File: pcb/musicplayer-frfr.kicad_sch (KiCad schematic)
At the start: 22 parts, among them J1 Battery, J2 AudioPlug3, J3 Display, SW1 SW_Push, SW2 SW_Push, SW3 SW_Push, SW4 RotaryEncoder_Switch, U1 XIAO-RP2350-SMD, U2 TP4056-42-ESOP8, U3 DFPLAYER_MINI

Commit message: fix up pcb with cool new rounded corners and some layout changes. also added a power switch
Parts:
- added SW5: SW_SPDT, Button_Switch_THT:SW_Slide_SPDT_Straight_CK_OS102011MS2Q, symbol Switch:SW_SPDT
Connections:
- net VBAT: now also SW5.1 (A); no longer U1.29 (VBAT)
- new net XIAO_VBAT: SW5.2 (B), U1.29 (VBAT)
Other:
- moved on the sheet: C3, C4, J2, U1

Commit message: fix up pcb bcuz kicad didnt place the right parts. also added fabrication files
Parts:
- C1, C2, C3: LCSC PN (none) -> C88722
- C4: value 0.1u -> 100n; LCSC PN (none) -> C1711
- D1, D2: LCSC PN (none) -> C5353439
- J1: LCSC PN (none) -> C157932
- J2: LCSC PN (none) -> C4991872
- J3: LCSC PN (none) -> C7191451; MPN (none) -> 68604-804HLF
- R1: LCSC PN (none) -> C114521
- R2, R3, R4: LCSC PN (none) -> C844939
- R5, R6: LCSC PN (none) -> C844941
- SW1, SW2, SW3: LCSC PN (none) -> C557612; MPN (none) -> TS4550CJ
- SW4: LCSC PN (none) -> C202365; MPN (none) -> EC11E18244AU
- SW5: LCSC PN (none) -> C221829; MPN (none) -> OS102011MS2QN1
- U1: LCSC PN (none) -> C41882923; MPN (none) -> 102010550
- U2: LCSC PN (none) -> C16581; MPN (none) -> TP4056-42-ESOP8
- U3: LCSC PN (none) -> C5371690; MPN (none) -> DFR0299

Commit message: rework schemtaic to bet bigger badder and better
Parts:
- removed C1, C2, C3: 100u, Capacitor_THT:CP_Radial_D6.3mm_P2.50mm, symbol Device:C
- removed C4: 100n, Capacitor_SMD:C_0805_2012Metric, symbol Device:C
- removed D1, D2: LED, LED_SMD:LED_0805_2012Metric, symbol Device:LED
- removed J2: AudioPlug3, Connector_Audio:Jack_3.5mm_CUI_SJ-3523-SMT_Horizontal, symbol Connector_Audio:AudioPlug3
- removed R1: 2.4K, Resistor_SMD:R_0805_2012Metric, symbol Device:R
- removed R2: 1K, Resistor_SMD:R_0805_2012Metric, symbol Device:R
- removed SW4: RotaryEncoder_Switch, Rotary_Encoder:RotaryEncoder_Alps_EC11E-Switch_Vertical_H20mm, symbol Device:RotaryEncoder_Switch
- removed U2: TP4056-42-ESOP8, Package_SO:SOIC-8-1EP_3.9x4.9mm_P1.27mm_EP2.41x3.3mm_ThermalVias, symbol Battery_Management:TP4056-42-ESOP8
- removed U3: DFPLAYER_MINI, DFPlayer:DFPlayer_V2, symbol Arduino:DFPLAYER_MINI
- added D1, D2, D3, D4, D5, D6, D7, D8, D9: 1N4149, Diode_THT:D_DO-35_SOD27_P7.62mm_Horizontal, symbol Diode:1N4149
- added R7: 4.7k, symbol Device:R
- added SW10: Next, Button_Switch_THT:SW_PUSH_6mm, symbol Switch:SW_Push
- added SW4: Left, Button_Switch_THT:SW_PUSH_6mm, symbol Switch:SW_Push
- added SW6: Select, Button_Switch_THT:SW_PUSH_6mm, symbol Switch:SW_Push
- added SW7: Right, Button_Switch_THT:SW_PUSH_6mm, symbol Switch:SW_Push
- added SW8: Prev., Button_Switch_THT:SW_PUSH_6mm, symbol Switch:SW_Push
- added SW9: Down, Button_Switch_THT:SW_PUSH_6mm, symbol Switch:SW_Push
- added TP1: USB D-, symbol Connector:TestPoint
- added TP2: USB D+, symbol Connector:TestPoint
- added U4: ESP32-S3-WROOM-1, RF_Module:ESP32-S3-WROOM-1, symbol RF_Module:ESP32-S3-WROOM-1
- R3: value 1K -> 10k; footprint Resistor_SMD:R_0805_2012Metric -> (none); LCSC PN C844939 -> (none); MPN CRCW08051K00FKEA -> (none)
- R4: value 1K -> 4.7k; footprint Resistor_SMD:R_0805_2012Metric -> (none); LCSC PN C844939 -> (none); MPN CRCW08051K00FKEA -> (none)
- SW1: value SW_Push -> Vol Up
- SW2: value SW_Push -> Up
- SW3: value SW_Push -> Vol Down
- SW5: value SW_SPDT -> SW_BAT
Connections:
- net ENCODER_SWITCH is gone; now on net XIAO_RX: U1.15 (D11)
- net +3V3: now also J3.3 (VCC), R3.1, R4.1, R7.1, U4.2 (3V3)
- net BUSY: now also U1.1 (D0); no longer U1.16 (D12)
- net GND: now also U4.1 (GND), U4.40 (GND), U4.41 (GND); no longer R3.1, SW1.2, SW2.2, SW3.2
- net SCL: now also R7.2
- net SDA: now also R4.2
- net XIAO_RX: now also U4.37 (TXD0); no longer U1.7 (D6)
- net XIAO_TX: now also U1.16 (D12), U4.36 (RXD0); no longer R4.1, U1.8 (D7)
- net SPI_MISO: now reaches U1.10 (D9)
- net SPI_MISO: now also U4.21 (IO13)
- net SPI_MOSI: now reaches U1.11 (D10)
- net SPI_MOSI: now also U4.19 (IO11)
- net COL2: now reaches U1.19 (D15)
- net COL2: now also SW2.1, SW6.1, SW9.1
- net COL1: now reaches U1.20 (D16)
- net COL1: now also SW1.1, SW4.1, SW8.1
- net ROW3: now reaches U1.21 (D17)
- net ROW3: now also D7.1 (K), D8.1 (K), D9.1 (K)
- net ROW2: now reaches U1.22 (D18)
- net ROW2: now also D4.1 (K), D5.1 (K), D6.1 (K)
- net SPI_CS: now reaches U1.4 (D3)
- net SPI_CS: now also U4.18 (IO10)
- net SPI_SCK: now reaches U1.9 (D8)
- net SPI_SCK: now also U4.20 (IO12)
- net ESP_BOOT: now reaches R3.2
- net ESP_BOOT: now also U4.27 (IO0)
- net BACK: no longer names the net of U1.3 (D2)
- net BACK: no longer SW1.1
- net ENCODER_A: no longer names the net of U1.17 (D13)
- net ENCODER_B: no longer names the net of U1.18 (D14)
- net NEXT renamed COL3
- net COL3: now also SW10.1, SW7.1
- removed net PLAY: SW2.1, U1.1 (D0)
- net VBUS renamed +5V
- net +5V: no longer J3.3 (VCC)
- new net: D1.2 (A), SW1.2
- new net: D8.2 (A), SW9.2
- new net: D9.2 (A), SW10.2
- new net: D2.2 (A), SW2.2
- new net: TP1.1, U4.13 (USB_D-)
- new net: D5.2 (A), SW6.2
- new net: D4.2 (A), SW4.2
- new net: D6.2 (A), SW7.2
- new net: D7.2 (A), SW8.2
- new net: D3.2 (A), SW3.2
- new net: TP2.1, U4.14 (USB_D+)
- new net AMP_SDN: U4.39 (IO1)
- new net DAC_XSMT: U4.12 (IO8)
- new net ESP_ENABLE: U1.7 (D6), U4.3 (EN)
- new net I2S_BCK: U4.31 (IO38)
- new net I2S_DIN: U4.32 (IO39)
- new net I2S_LRCK: U4.33 (IO40)
- new net ROW1: D1.1 (K), D2.1 (K), D3.1 (K), U1.8 (D7)
- new net SD_CLK: U4.22 (IO14)
- new net SD_CMD: U4.8 (IO15)
- new net SD_D0: U4.38 (IO2)
- new net SD_D1: U4.4 (IO4)
- new net SD_D2: U4.5 (IO5)
- new net SD_D3: U4.6 (IO6)
- new net SD_DET: U4.7 (IO7)
- no-connect marks 19 -> 2
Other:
- added sheet Audio (audio.kicad_sch)
- added sheet SD Card (sd.kicad_sch)
- note added: "User Controls"
- moved on the sheet: J1, J3, R5, R6, SW1, SW2, SW3, SW5

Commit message: add RTC and stuff
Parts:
- added TP3, TP4, TP5, TP6: TestPoint, symbol Connector:TestPoint
- added U5: PCF8523T, Package_SO:SOIC-8_3.9x4.9mm_P1.27mm, symbol Timer_RTC:PCF8523T
- added Y1: 32.768 kHz, symbol Device:Crystal
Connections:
- net +3V3: now also TP6.1
- net +5V: now also TP4.1, U5.8 (VDD)
- net GND: now also TP3.1, U5.4 (VSS)
- net SCL: now also U5.6 (SCL)
- net SDA: now also U5.5 (SDA)
- net VBAT: now also TP5.1, U5.3 (VBAT)
- net INTA: now reaches U1.17 (D13)
- net INTA: now also U5.7 (~{INT1}/CLKOUT)
- net BUSY: no longer names the net of U1.1 (D0)
- new net: U5.1 (OSCI), Y1.1
- new net: U5.2 (OSCO), Y1.2
- no-connect marks 2 -> 22
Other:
- note added: "Audio"
- note added: "Battery stuff"
- note added: "Display"
- note added: "ESP32"
- note added: "RTC"
- note added: "SD Card"
- note added: "XIAO RP2350"
- moved on the sheet: D1, D2, D3, D4, D5, D6, D7, D8, D9, J1, J3, R3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

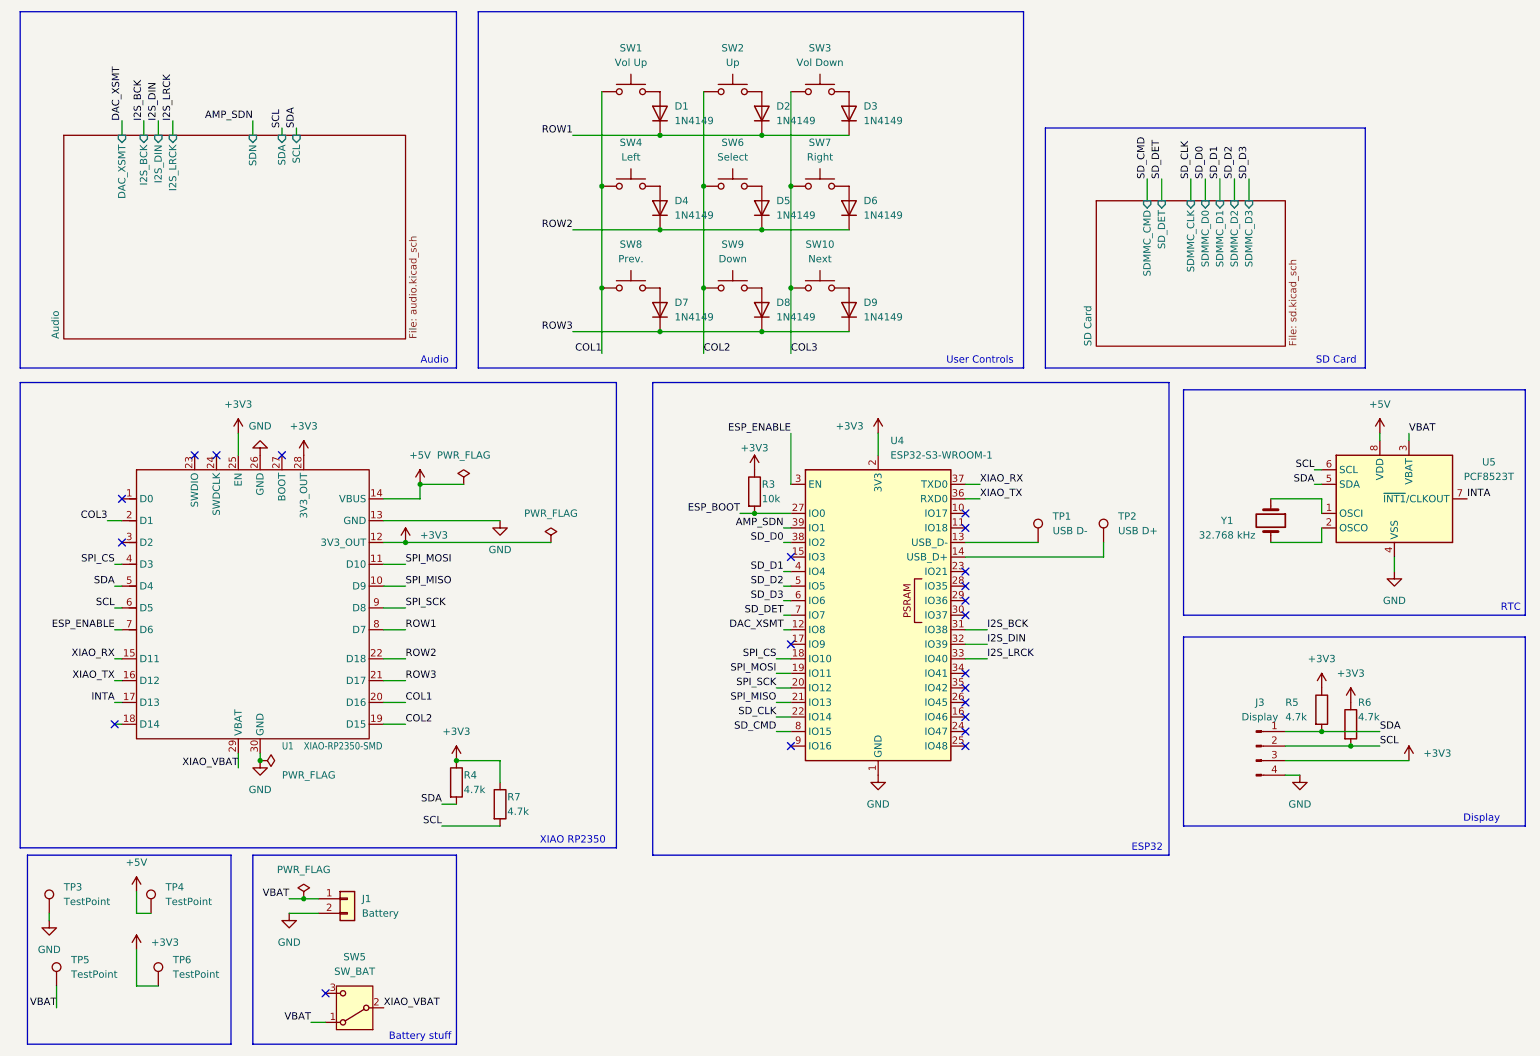
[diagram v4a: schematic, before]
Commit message: fix JOURNAL.md hour formatting
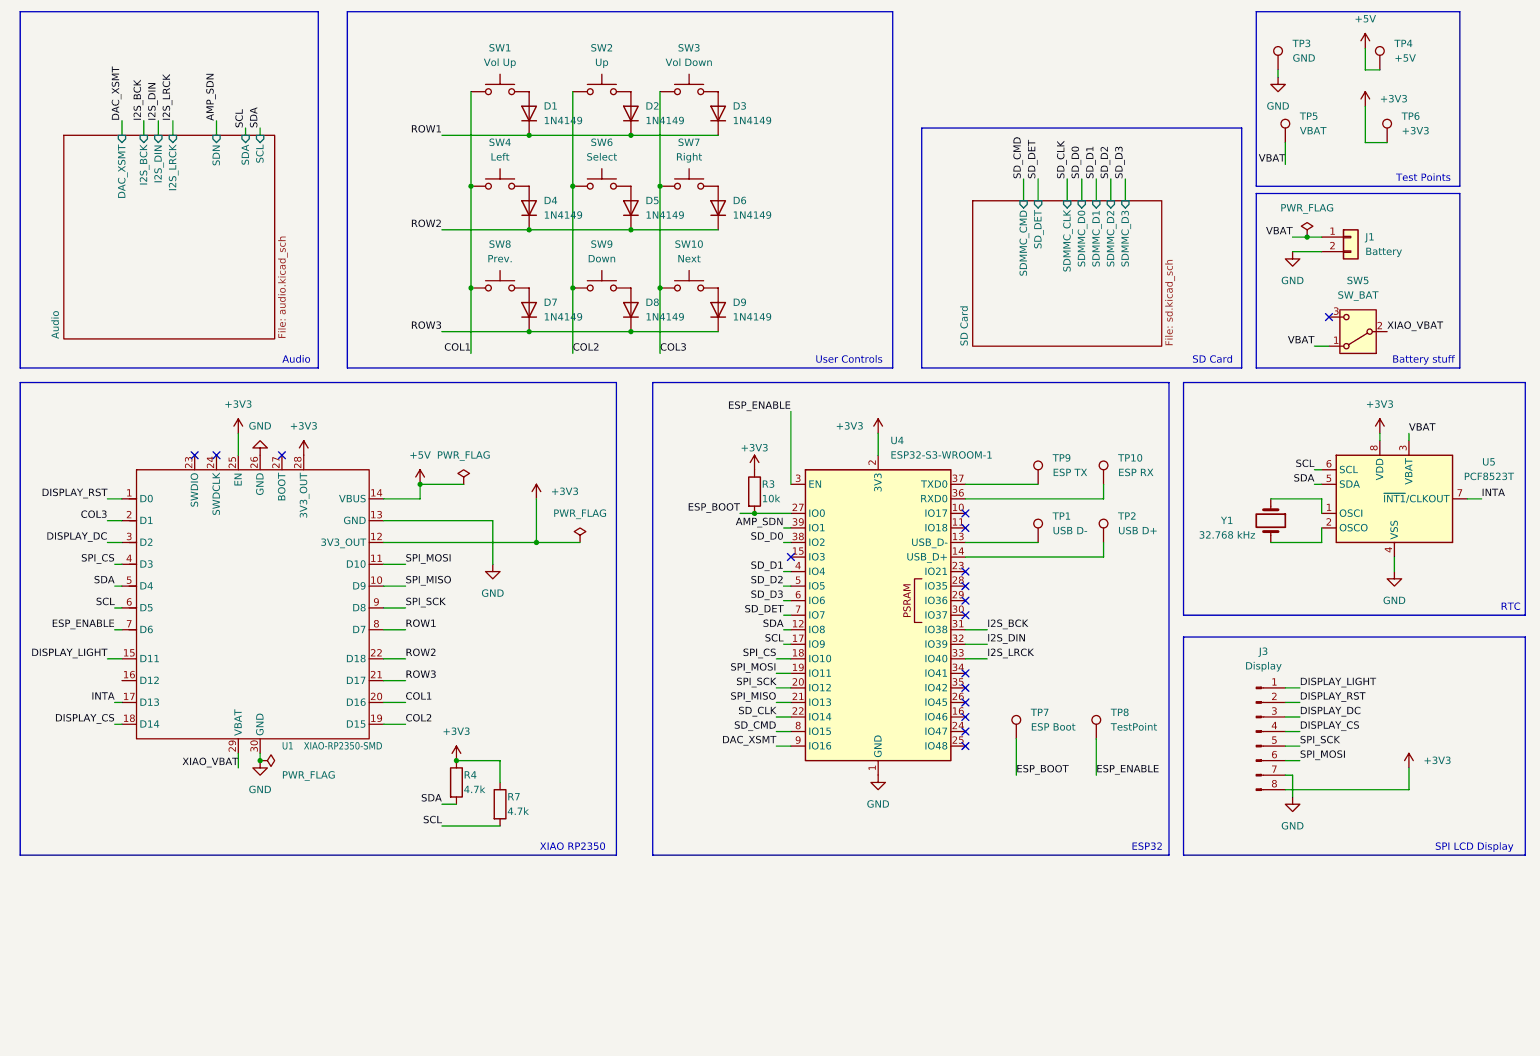
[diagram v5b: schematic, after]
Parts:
- removed J3: Display, Connector_PinHeader_2.54mm:PinHeader_1x04_P2.54mm_Vertical, symbol Connector:Conn_01x04_Pin
- removed R5, R6: 4.7k, Resistor_SMD:R_0805_2012Metric, symbol Device:R
- added J3: Display, symbol Connector:Conn_01x08_Pin
- added TP10: ESP RX, symbol Connector:TestPoint
- added TP7: ESP Boot, symbol Connector:TestPoint
- added TP8: TestPoint, symbol Connector:TestPoint
- added TP9: ESP TX, symbol Connector:TestPoint
- TP3: value TestPoint -> GND
- TP4: value TestPoint -> +5V
- TP5: value TestPoint -> VBAT
- TP6: value TestPoint -> +3V3
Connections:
- net +3V3: now also U5.8 (VDD), J3.8 (Pin_8)
- net +5V: no longer U5.8 (VDD)
- net DAC_XSMT: now also U4.9 (IO16); no longer U4.12 (IO8)
- net ESP_BOOT: now also TP7.1
- net ESP_ENABLE: now also TP8.1
- net GND: now also J3.7 (Pin_7)
- net SCL: now also U4.17 (IO9)
- net SDA: now also U4.12 (IO8)
- net SPI_MOSI: now also J3.6 (Pin_6)
- net SPI_SCK: now also J3.5 (Pin_5)
- net DISPLAY_RST: now reaches U1.1 (D0)
- net DISPLAY_RST: now also J3.2 (Pin_2)
- net DISPLAY_CS: now reaches U1.18 (D14)
- net DISPLAY_CS: now also J3.4 (Pin_4)
- net DISPLAY_DC: now reaches U1.3 (D2)
- net DISPLAY_DC: now also J3.3 (Pin_3)
- net XIAO_RX: no longer names the net of U4.37 (TXD0)
- net XIAO_RX: now also TP9.1; no longer U1.15 (D11)
- net XIAO_TX: no longer names the net of U1.16 (D12)
- net XIAO_TX: no longer U4.36 (RXD0)
- new net: TP10.1, U4.36 (RXD0)
- new net DISPLAY_LIGHT: J3.1 (Pin_1), U1.15 (D11)
- no-connect marks 22 -> 17
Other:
- note added: "SPI LCD Display"
- note added: "Test Points"
- note removed: "Display"
- moved on the sheet: D1, D2, D3, D4, D5, D6, D7, D8, D9, SW1, SW10, SW2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

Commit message: layout pcb
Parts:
- J3: footprint (none) -> Connector_PinHeader_2.54mm:PinHeader_1x08_P2.54mm_Vertical
- R3, R4, R7: footprint (none) -> Resistor_SMD:R_0805_2012Metric_Pad1.20x1.40mm_HandSolder
- TP1, TP10, TP2, TP3, TP4, TP5, TP6, TP7, TP9: footprint (none) -> TestPoint:TestPoint_Pad_D3.0mm
- TP8: value TestPoint -> ESP Enable; footprint (none) -> TestPoint:TestPoint_Pad_D3.0mm
- Y1: footprint (none) -> Crystal:Crystal_SMD_2012-2Pin_2.0x1.2mm_HandSoldering
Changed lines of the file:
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@@
 			)
 		)
-		(property "Value" "TestPoint"
+		(property "Value" "ESP Enable"
 			(at 204.47 140.2079 0)
 			(show_name no)
@@
 			)
 		)
-		(property "Footprint" ""
+		(property "Footprint" "TestPoint:TestPoint_Pad_D3.0mm"
 			(at 207.01 142.24 0)
 			(hide yes)
@@
 			)
 		)
-		(property "Footprint" ""
+		(property "Footprint" "Crystal:Crystal_SMD_2012-2Pin_2.0x1.2mm_HandSoldering"
 			(at 232.41 104.14 0)
 			(hide yes)
@@
 			)
 		)
-		(property "Footprint" ""
+		(property "Footprint" "Resistor_SMD:R_0805_2012Metric_Pad1.20x1.40mm_HandSolder"
 			(at 140.462 99.06 90)
 			(hide yes)
@@
 			)
 		)
-		(property "Footprint" ""
+		(property "Footprint" "Connector_PinHeader_2.54mm:PinHeader_1x08_P2.54mm_Vertical"
 			(at 229.87 140.97 0)
 			(hide yes)
@@
 			)
 		)
+		(property "MPN" ""
+			(at 229.87 140.97 0)
+			(hide yes)
+			(show_name no)
+			(do_not_autoplace no)
+			(effects
+				(font
+					(size 1.27 1.27)
+				)
+			)
+		)
+		(property "LCSC PN" ""
+			(at 229.87 140.97 0)
+			(hide yes)
+			(show_name no)
+			(do_not_autoplace no)
+			(effects
+				(font
+					(size 1.27 1.27)
+				)
+			)
+		)
 		(pin "2"
 		)
@@
 			)
 		)
-		(property "Footprint" ""
+		(property "Footprint" "TestPoint:TestPoint_Pad_D3.0mm"
 			(at 208.28 97.79 0)
 			(hide yes)
@@
 			)
 		)
-		(property "Footprint" ""
+		(property "Footprint" "TestPoint:TestPoint_Pad_D3.0mm"
 			(at 238.76 25.4 0)
 			(hide yes)
@@
 			)
 		)
-		(property "Footprint" ""
+		(property "Footprint" "TestPoint:TestPoint_Pad_D3.0mm"
 			(at 256.54 25.4 0)
 			(hide yes)
@@
 			)
 		)
-		(property "Footprint" ""
+		(property "Footprint" "TestPoint:TestPoint_Pad_D3.0mm"
 			(at 196.85 107.95 0)
 			(hide yes)
@@
 			)
 		)
-		(property "Footprint" ""
+		(property "Footprint" "TestPoint:TestPoint_Pad_D3.0mm"
 			(at 196.85 97.79 0)
 			(hide yes)
@@
 			)
 		)
-		(property "Footprint" ""
+		(property "Footprint" "Resistor_SMD:R_0805_2012Metric_Pad1.20x1.40mm_HandSolder"
 			(at 88.392 149.86 90)
 			(hide yes)
@@
 			)
 		)
-		(property "Footprint" ""
+		(property "Footprint" "Resistor_SMD:R_0805_2012Metric_Pad1.20x1.40mm_HandSolder"
 			(at 96.012 153.67 90)
 			(hide yes)
@@
 			)
 		)
-		(property "Footprint" ""
+		(property "Footprint" "TestPoint:TestPoint_Pad_D3.0mm"
 			(at 193.04 142.24 0)
 			(hide yes)
@@
 			)
 		)
-		(property "Footprint" ""
+		(property "Footprint" "TestPoint:TestPoint_Pad_D3.0mm"
 			(at 208.28 107.95 0)
 			(hide yes)
@@
 			)
 		)
-		(property "Footprint" ""
+		(property "Footprint" "TestPoint:TestPoint_Pad_D3.0mm"
 			(at 257.81 38.1 0)
 			(hide yes)
@@
 			)
 		)
-		(property "Footprint" ""
+		(property "Footprint" "TestPoint:TestPoint_Pad_D3.0mm"
 			(at 240.03 38.1 0)
 			(hide yes)
